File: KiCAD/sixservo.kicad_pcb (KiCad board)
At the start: 2 copper layers, 43.2 x 43.2 mm, 40 parts, among them J0 ICSP, J1 USB_to_TTL, J21 servo1, J22 servo2, J23 servo3, J24 servo4, J25 servo5, J26 servo6, J33 i2c-3.3, J332 i2c-3.3_2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

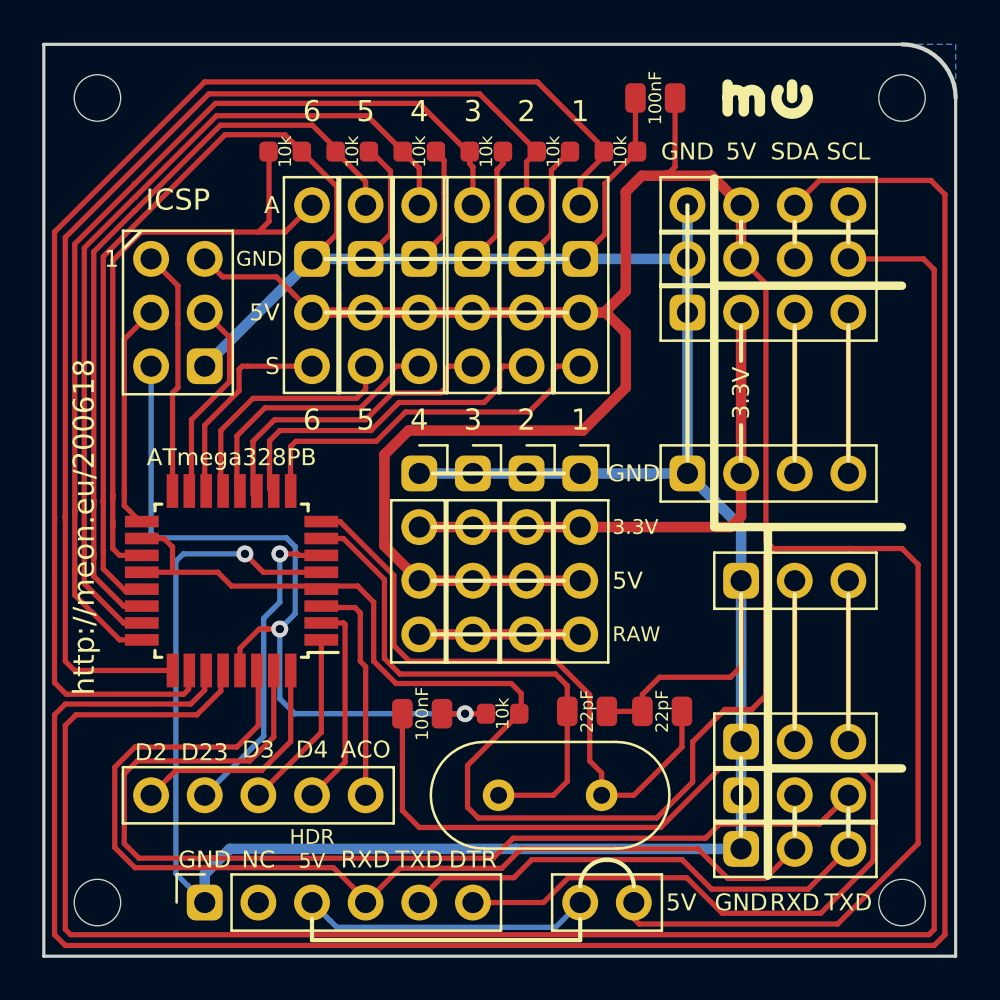
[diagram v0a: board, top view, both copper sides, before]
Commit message: s/ATmega328PB/ATmega328P/, add TX/RX protective resistors
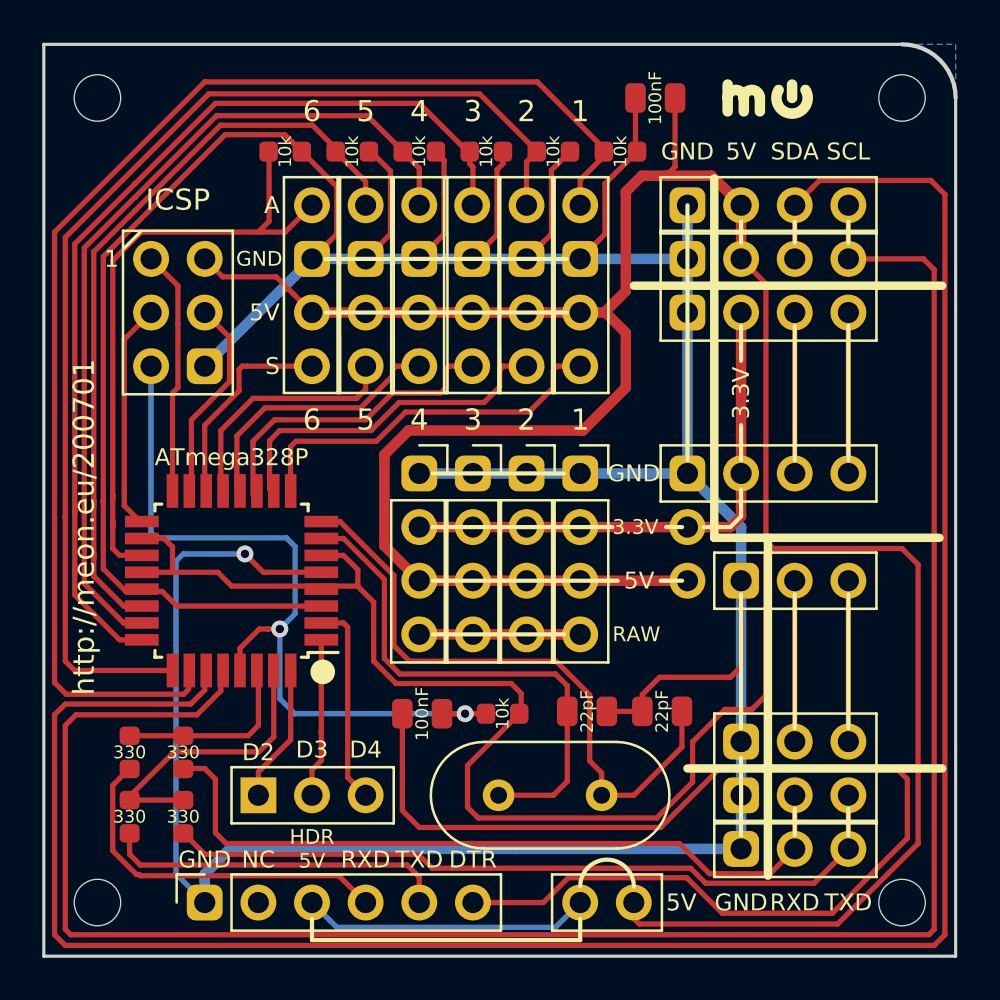
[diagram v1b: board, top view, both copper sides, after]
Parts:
- added J97: Power, Connector_PinSocket_2.54mm:PinSocket_1x02_P2.54mm_Vertical_no_lines, F.Cu at (119.4, 175.3)
- added R12: 330, Resistor_SMD (GitHub):R_0603_1608Metric_no_lines, F.Cu at (93.0, 185.9)
- added R13: 330, Resistor_SMD (GitHub):R_0603_1608Metric_no_lines, F.Cu at (93.0, 189.0)
- added R14: 330, Resistor_SMD (GitHub):R_0603_1608Metric_no_lines, F.Cu at (95.5, 185.9)
- added R15: 330, Resistor_SMD (GitHub):R_0603_1608Metric_no_lines, F.Cu at (95.5, 189.0)
- J5: footprint Connector_PinSocket_2.54mm:PinSocket_1x05_P2.54mm_Vertical_closed -> Connector_PinSocket_2.54mm:PinSocket_1x03_P2.54mm_Vertical_closed
- U1: value ATmega328PB-AU -> ATmega328P-AU
- moved J5 5.08 mm to (99.1, 188.0)
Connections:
- J1 pad 4: RXD -> Net-(J1-Pad4)
- J1 pad 5: TXD -> Net-(J1-Pad5)
- J45 pad 2: RXD -> RXD_P
- J45 pad 3: TXD -> TXD_P
- J452 pad 2: RXD -> RXD_P
- J452 pad 3: TXD -> TXD_P
- J5 pad 2: D23 -> D3
- J5 pad 3: D3 -> D4
- U1 pad 3: ACO -> GND
- U1 pad 6: D23 -> +5V
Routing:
- net TXD: track 75.8 -> 13.9 mm
- net RXD: track 51.9 -> 8.84 mm
- net RXD_P: track 0.00 -> 36.7 mm
- net TXD_P: track 0.00 -> 35.7 mm
- net Net-(J1-Pad4): track 0.00 -> 17.2 mm
- net Net-(J1-Pad5): track 0.00 -> 16.4 mm
- net D23: track 14.9 -> 0.00 mm, vias 1 -> 0
- net ACO: track 10.6 -> 0.00 mm
- net GND: track 199.6 -> 208.2 mm
- net +5V: track 177.2 -> 185.1 mm
- net D2: track 11.0 -> 6.54 mm
- net DTR: track 53.5 -> 56.2 mm
- net D3: track 8.59 -> 7.61 mm
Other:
- board text added: "ATmega328P"
- board text added: "http://meon.eu/200701"
- board text removed: "ACO"
- board text removed: "ATmega328PB"
- board text removed: "D23"
- board text removed: "http://meon.eu/200618"

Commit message: add raw+gnd pins for power shield
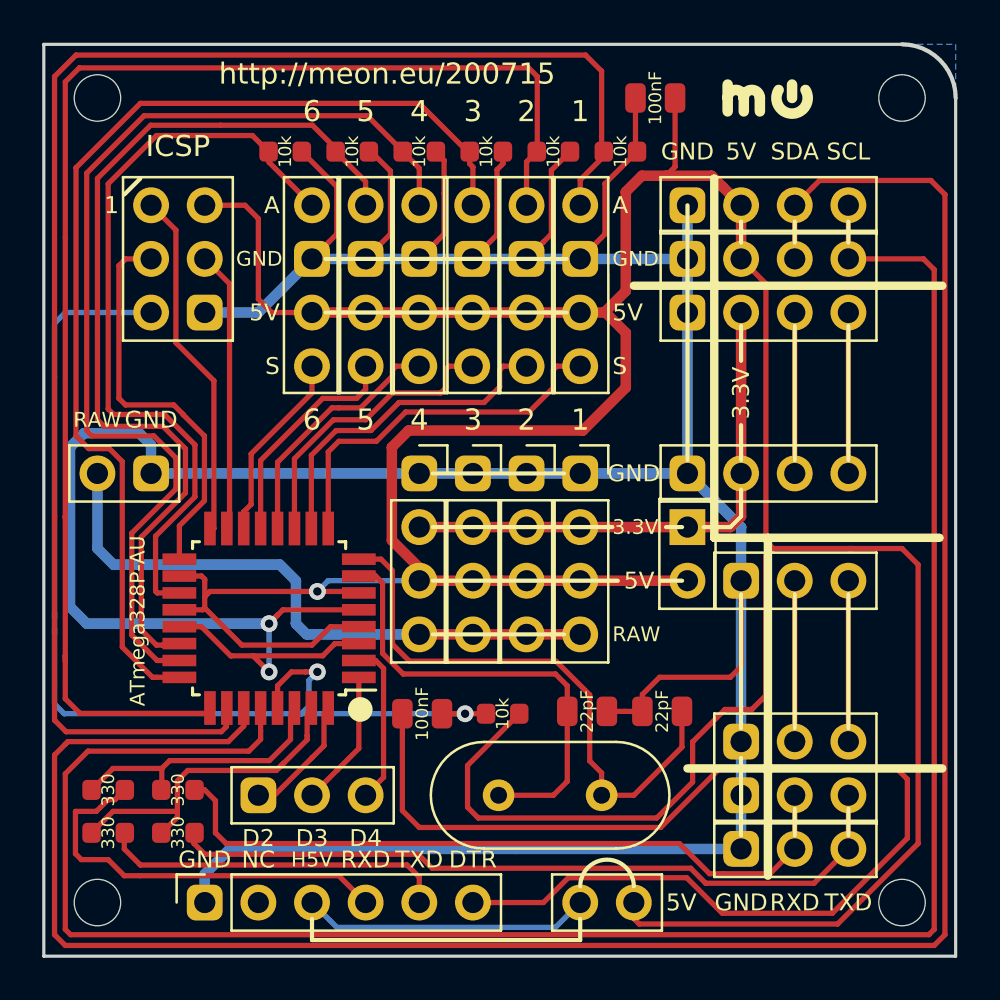
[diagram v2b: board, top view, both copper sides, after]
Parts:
- added J95: Power, Connector_PinHeader_2.54mm:PinHeader_1x02_P2.54mm_Vertical_closed, F.Cu at (94.0, 172.7)
- J97: footprint Connector_PinSocket_2.54mm:PinSocket_1x02_P2.54mm_Vertical_no_lines -> Connector_PinHeader_2.54mm:PinHeader_1x02_P2.54mm_Vertical_closed
- moved J0 2.54 mm to (94.0, 160.0)
- moved U1 2.51 mm to (99.6, 179.6)
- moved R12 2.05 mm to (91.9, 187.7), turned to 0 degrees
- moved R14 1.80 mm to (95.2, 187.7), turned to 0 degrees
- moved R13 1.27 mm to (91.9, 189.7), turned to 0 degrees
- moved R15 0.80 mm to (95.2, 189.7), turned to 0 degrees
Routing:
- net RAW: track 7.62 -> 29.3 mm
- net ~RST: track 37.0 -> 50.6 mm
- net A2: track 54.5 -> 65.8 mm
- net A3: track 62.0 -> 73.1 mm
- net GND: track 208.2 -> 198.6 mm, vias 1 -> 2
- net A0: track 40.7 -> 48.6 mm
- net A7: track 36.3 -> 44.2 mm
- net D13_SCK: track 11.3 -> 19.1 mm
- net A6: track 30.1 -> 36.8 mm
- net D12_MISO: track 11.8 -> 16.8 mm
- net A1: track 45.9 -> 50.5 mm
- net D11_MOSI: track 9.67 -> 13.5 mm
- net RXD: track 8.84 -> 12.6 mm
- net Net-(C11-Pad2): track 24.7 -> 21.8 mm
- net Net-(C12-Pad1): track 29.5 -> 27.1 mm
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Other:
- board text added: "H5V"
- board text added: "http://meon.eu/200715"
- board text removed: "ATmega328P"
- board text removed: "HDR 5V"
- board text removed: "http://meon.eu/200701"
